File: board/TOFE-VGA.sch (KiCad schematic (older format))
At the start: 0 parts

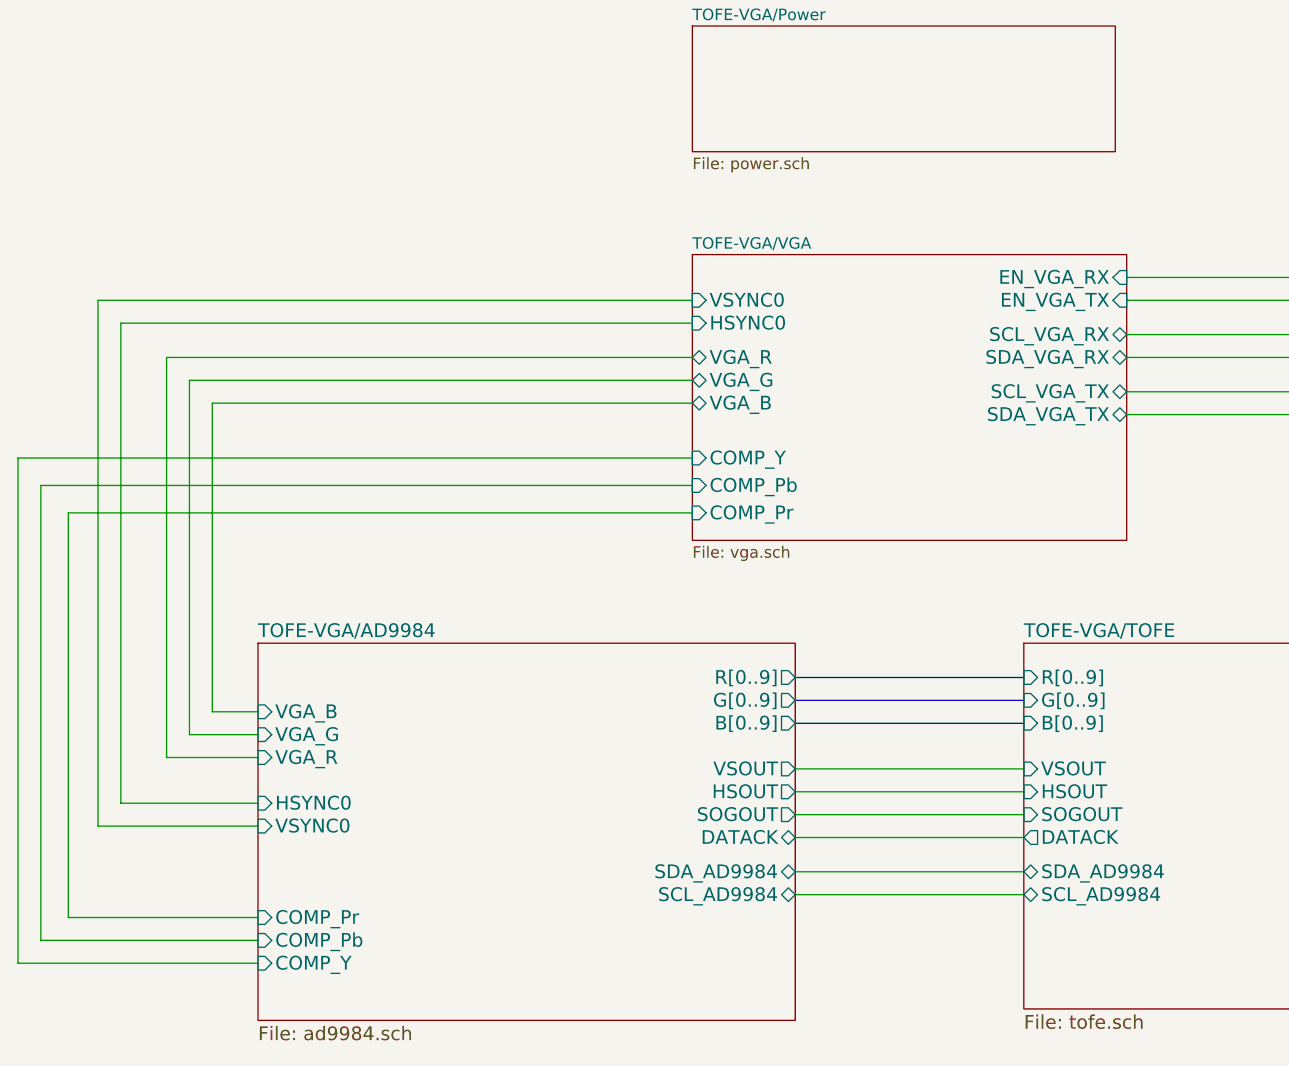
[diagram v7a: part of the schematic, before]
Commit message: Adding a way to disconnect the output from the input.
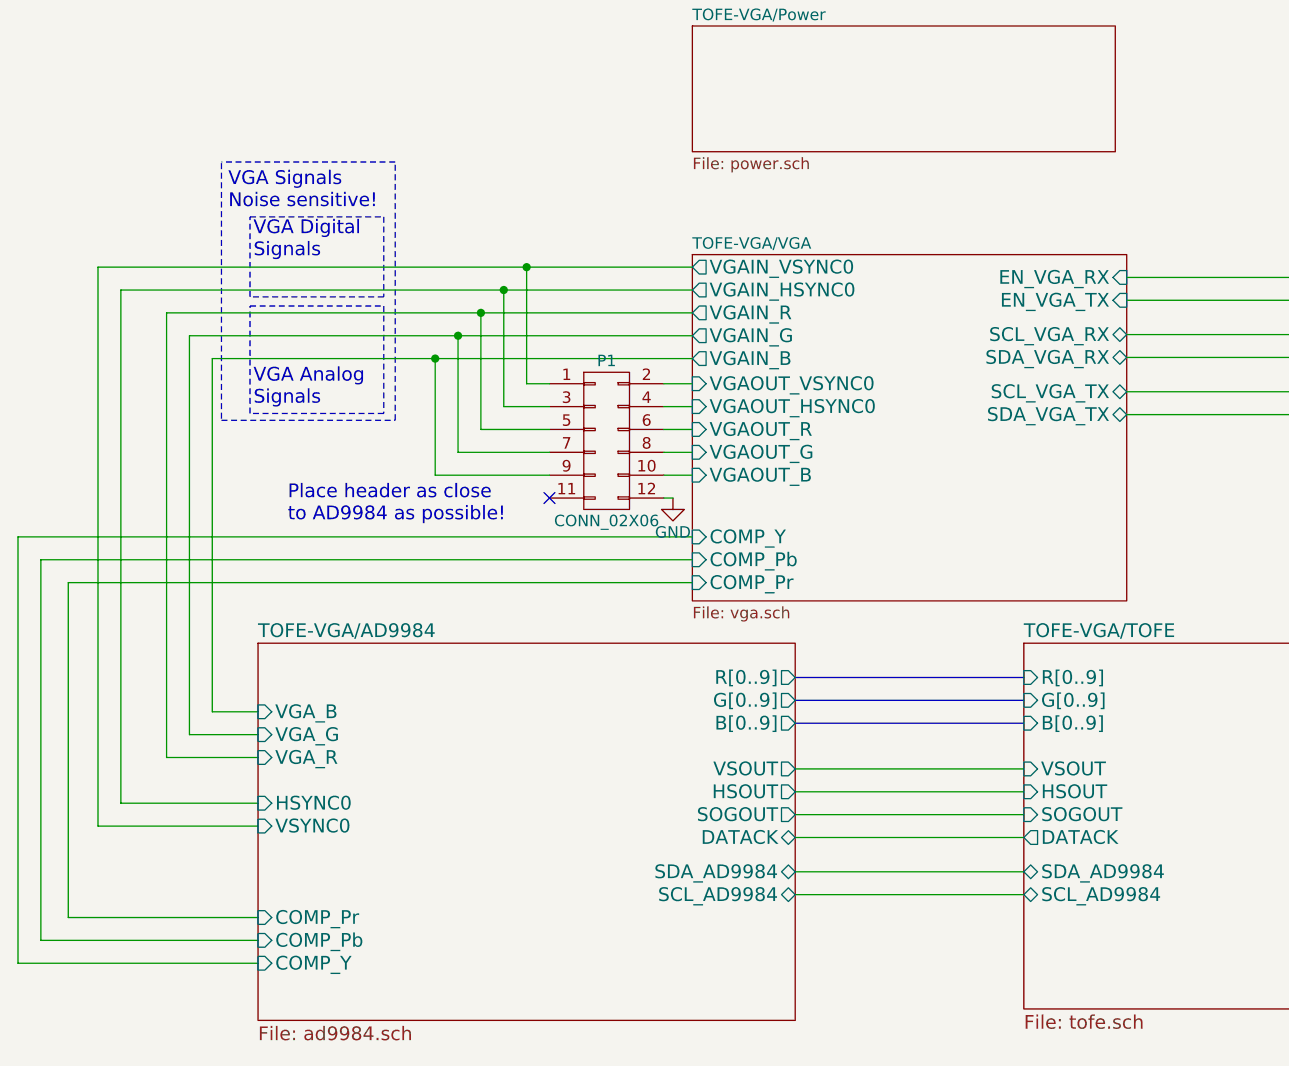
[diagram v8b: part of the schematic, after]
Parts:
- added P1: CONN_02X06, Pin_Headers:Pin_Header_Straight_2x06, symbol CONN_02X06
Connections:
- net TOFE-VGA/AD9984/HSYNC0: now also P1.3 (P3)
- net TOFE-VGA/AD9984/VGA_B: now also P1.9 (P9)
- net TOFE-VGA/AD9984/VGA_G: now also P1.7 (P7)
- net TOFE-VGA/AD9984/VGA_R: now also P1.5 (P5)
- net TOFE-VGA/AD9984/VSYNC0: now also P1.1 (P1)
- new net GND: P1.12 (P12)
- new net TOFE-VGA/VGA/VGAOUT_B: P1.10 (P10)
- new net TOFE-VGA/VGA/VGAOUT_G: P1.8 (P8)
- new net TOFE-VGA/VGA/VGAOUT_HSYNC0: P1.4 (P4)
- new net TOFE-VGA/VGA/VGAOUT_R: P1.6 (P6)
- new net TOFE-VGA/VGA/VGAOUT_VSYNC0: P1.2 (P2)
- no-connect marks 0 -> 1
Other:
- note added: "Place header as close \nto AD9984 as possible!"
- note added: "VGA Analog\nSignals"
- note added: "VGA Digital\nSignals"
- note added: "VGA Signals\nNoise sensitive!"
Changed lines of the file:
@@
 $EndSheet
 $Sheet
-S 5100 2150 1900 1250
+S 5100 2150 1900 1515
 U 563EFC3B
 F0 "TOFE-VGA/VGA" 50
@@
 F4 "SCL_VGA_TX" B R 7000 2750 60
 F5 "SDA_VGA_TX" B R 7000 2850 60
-F6 "VGA_B" B L 5100 2800 60
-F7 "VGA_G" B L 5100 2700 60
-F8 "VGA_R" B L 5100 2600 60
-F9 "HSYNC0" I L 5100 2450 60
-F10 "VSYNC0" I L 5100 2350 60
+F6 "VGAIN_B" O L 5100 2605 60
+F7 "VGAIN_G" O L 5100 2505 60
+F8 "VGAIN_R" O L 5100 2405 60
+F9 "VGAIN_HSYNC0" O L 5100 2305 60
+F10 "VGAIN_VSYNC0" O L 5100 2205 60
 F11 "EN_VGA_RX" I R 7000 2250 60
 F12 "EN_VGA_TX" I R 7000 2350 60
-F13 "COMP_Y" I L 5100 3040 60
-F14 "COMP_Pb" I L 5100 3160 60
-F15 "COMP_Pr" I L 5100 3280 60
+F13 "COMP_Y" I L 5100 3385 60
+F14 "COMP_Pb" I L 5100 3485 60
+F15 "COMP_Pr" I L 5100 3585 60
+F16 "VGAOUT_B" I L 5100 3115 60
+F17 "VGAOUT_G" I L 5100 3015 60
+F18 "VGAOUT_R" I L 5100 2915 60
+F19 "VGAOUT_HSYNC0" I L 5100 2815 60
+F20 "VGAOUT_VSYNC0" I L 5100 2715 60
 $EndSheet
+$Comp
+L CONN_02X06 P1
+U 1 1 579CCE5F
+P 4725 2965
+F 0 "P1" H 4725 3315 50  0000 C CNN
+F 1 "CONN_02X06" H 4725 2615 50  0000 C CNN
+F 2 "Pin_Headers:Pin_Header_Straight_2x06" H 4725 1765 50  0001 C CNN
+F 3 "" H 4725 1765 50  0000 C CNN
+	1    4725 2965
+	1    0    0    -1
+$EndComp
+$Comp
+L GND #PWR01
+U 1 1 579D1C68
+P 5015 3215
+F 0 "#PWR01" H 5015 2965 50  0001 C CNN
+F 1 "GND" H 5015 3065 50  0000 C CNN
+F 2 "" H 5015 3215 50  0000 C CNN
+F 3 "" H 5015 3215 50  0000 C CNN
+	1    5015 3215
+	1    0    0    -1
+$EndComp
 Wire Wire Line
 	7000 2850 9450 2850
@@
 	3200 4150 3000 4150
 Wire Wire Line
-	3000 4150 3000 2800
-Wire Wire Line
-	2900 2700 2900 4250
+	3000 4150 3000 2605
+Wire Wire Line
+	2900 2505 2900 4250
 Wire Wire Line
 	2900 4250 3200 4250
@@
 	3200 4350 2800 4350
 Wire Wire Line
-	2800 4350 2800 2600
+	2800 4350 2800 2405
 Wire Wire Line
 	5550 4400 6550 4400
@@
 	5550 4950 6550 4950
 Wire Wire Line
-	3000 2800 5100 2800
-Wire Wire Line
-	5100 2700 2900 2700
-Wire Wire Line
-	2800 2600 5100 2600
-Wire Wire Line
-	5100 2450 2600 2450
-Wire Wire Line
-	2500 2350 5100 2350
+	3000 2605 5100 2605
+Wire Wire Line
+	2900 2505 5100 2505
+Wire Wire Line
+	2800 2405 5100 2405
+Wire Wire Line
+	2600 2305 5100 2305
+Wire Wire Line
+	2500 2205 5100 2205
 Wire Bus Line
 	5550 4000 6550 4000
@@
 	2500 4650 3200 4650
 Wire Wire Line
-	2500 2350 2500 4650
-Wire Wire Line
-	2600 4550 2600 2450
+	2500 2205 2500 4650
+Wire Wire Line
+	2600 4550 2600 2305
 Wire Wire Line
 	2150 5250 3200 5250
@@
 	10100 2250 7000 2250
 Wire Wire Line
-	2370 5050 2370 3280
-Wire Wire Line
-	2370 3280 5100 3280
-Wire Wire Line
-	2250 5150 2250 3160
-Wire Wire Line
-	2250 3160 5100 3160
-Wire Wire Line
-	2150 5250 2150 3040
-Wire Wire Line
-	2150 3040 5100 3040
+	2370 5050 2370 3585
+Wire Wire Line
+	2370 3585 5100 3585
+Wire Wire Line
+	2250 5150 2250 3485
+Wire Wire Line
+	2250 3485 5100 3485
+Wire Wire Line
+	2150 5250 2150 3385
+Wire Wire Line
+	2150 3385 5100 3385
+Wire Wire Line
+	5100 2715 4975 2715
+Wire Wire Line
+	5100 2815 4975 2815
+Wire Wire Line
+	4975 2915 5100 2915
+Wire Wire Line
+	4975 3015 5100 3015
+Wire Wire Line
+	4975 3115 5100 3115
+Wire Wire Line
+	5015 3215 4975 3215
+Wire Wire Line
+	4475 2715 4375 2715
+Wire Wire Line
+	4375 2715 4375 2205
+Connection ~ 4375 2205
+Wire Wire Line
+	4475 2815 4275 2815
+Wire Wire Line
+	4275 2815 4275 2305
+Connection ~ 4275 2305
+Wire Wire Line
+	4475 2915 4175 2915
+Wire Wire Line
+	4175 2915 4175 2405
+Connection ~ 4175 2405
+Wire Wire Line
+	4475 3015 4075 3015
+Wire Wire Line
+	4075 3015 4075 2505
+Connection ~ 4075 2505
+Wire Wire Line
+	4475 3115 3975 3115
+Wire Wire Line
+	3975 3115 3975 2605
+Connection ~ 3975 2605
+Wire Notes Line
+	3040 1750 3040 2875
+Wire Notes Line
+	3040 2875 3800 2875
+Wire Notes Line
+	3800 2875 3800 1745
+Wire Notes Line
+	3800 1745 3040 1745
+Text Notes 3070 1955 0    60   ~ 0
+VGA Signals\nNoise sensitive!
+Wire Notes Line
+	3750 2375 3750 2845
+Wire Notes Line
+	3750 2845 3165 2845
+Wire Notes Line
+	3165 2845 3165 2375
+Wire Notes Line
+	3165 2375 3750 2375
+Text Notes 3180 2815 0    60   ~ 0
+VGA Analog\nSignals
+NoConn ~ 4475 3215
+Text Notes 3330 3325 0    60   ~ 0
+Place header as close \nto AD9984 as possible!
+Text Notes 3180 2170 0    60   ~ 0
+VGA Digital\nSignals
+Wire Notes Line
+	3750 2335 3165 2335
+Wire Notes Line
+	3165 2335 3165 1985
+Wire Notes Line
+	3165 1985 3750 1985
+Wire Notes Line
+	3750 1985 3750 2335
 $EndSCHEMATC
